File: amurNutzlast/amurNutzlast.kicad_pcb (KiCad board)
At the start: 2 copper layers, 90 parts, among them J1 Conn_01x08, J2 USB_A, J3 Conn_01x02, J5 Conn_01x07, J6 Conn_01x06, J7 Conn_01x07, J8 Conn_01x20, U1 ICE40HX1K-TQ144, U3 LD1117S33TR_SOT223, U4 FT2232HL, U5 93LCxxA, U6 W25Q128JVS, X1 SG-7050CAN, Y1 12MHz

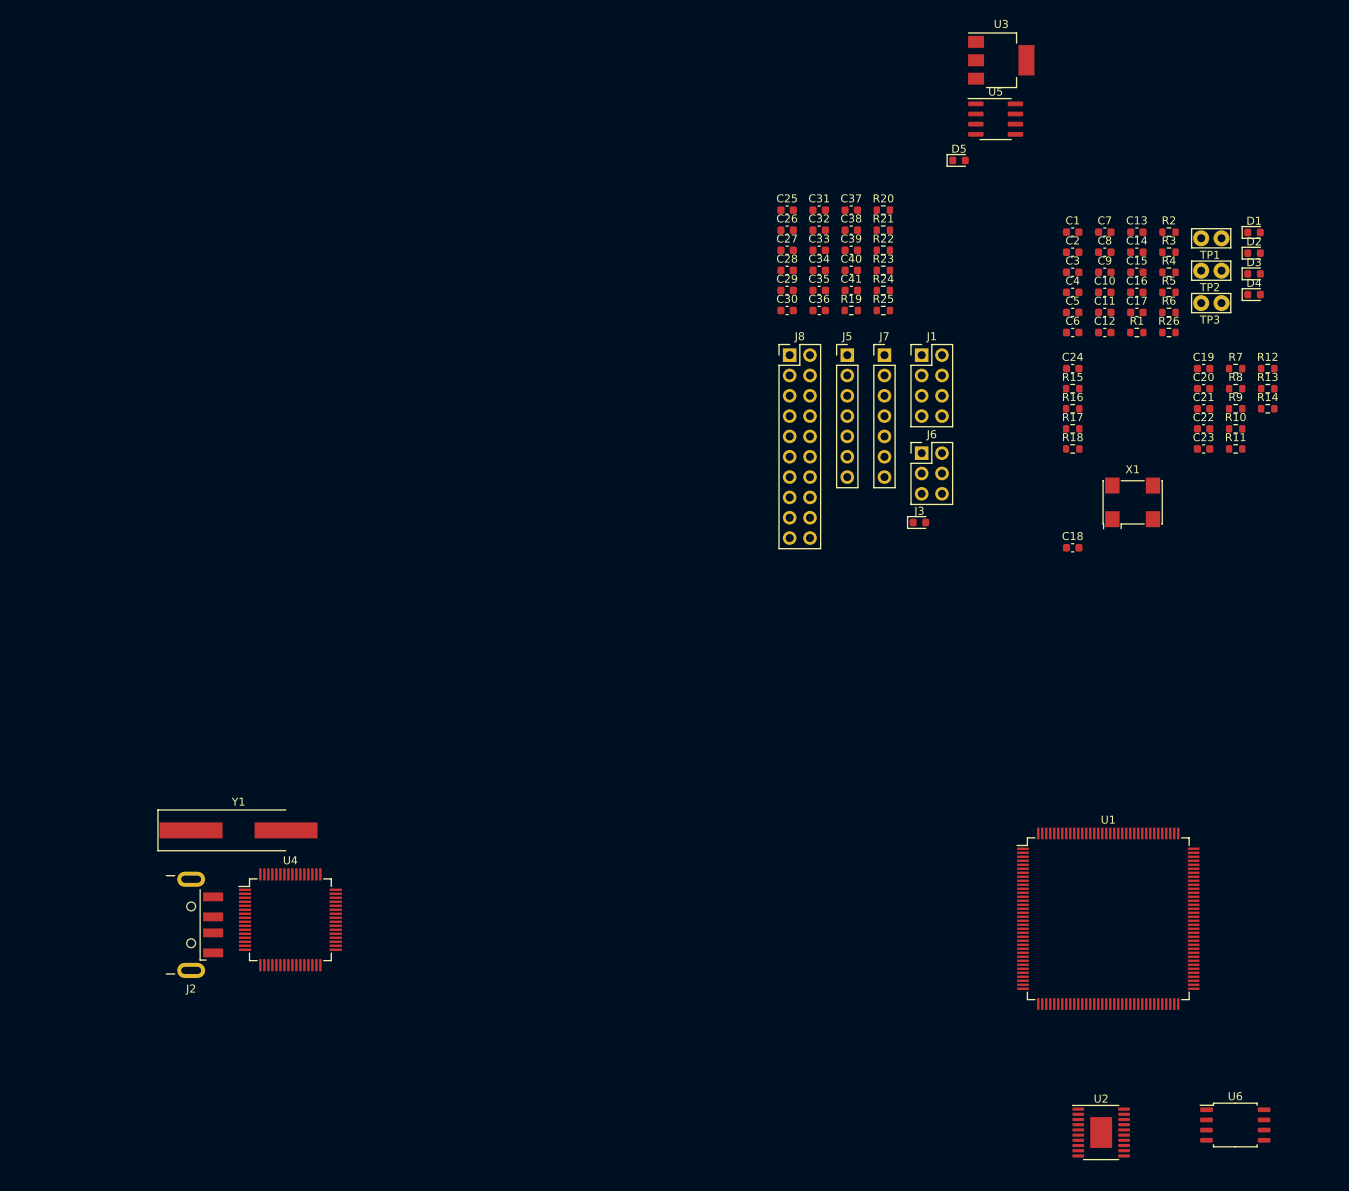
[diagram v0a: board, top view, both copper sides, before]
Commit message: deleted 3.3 converter for ftdi and moved USB to a hierarhical sheet
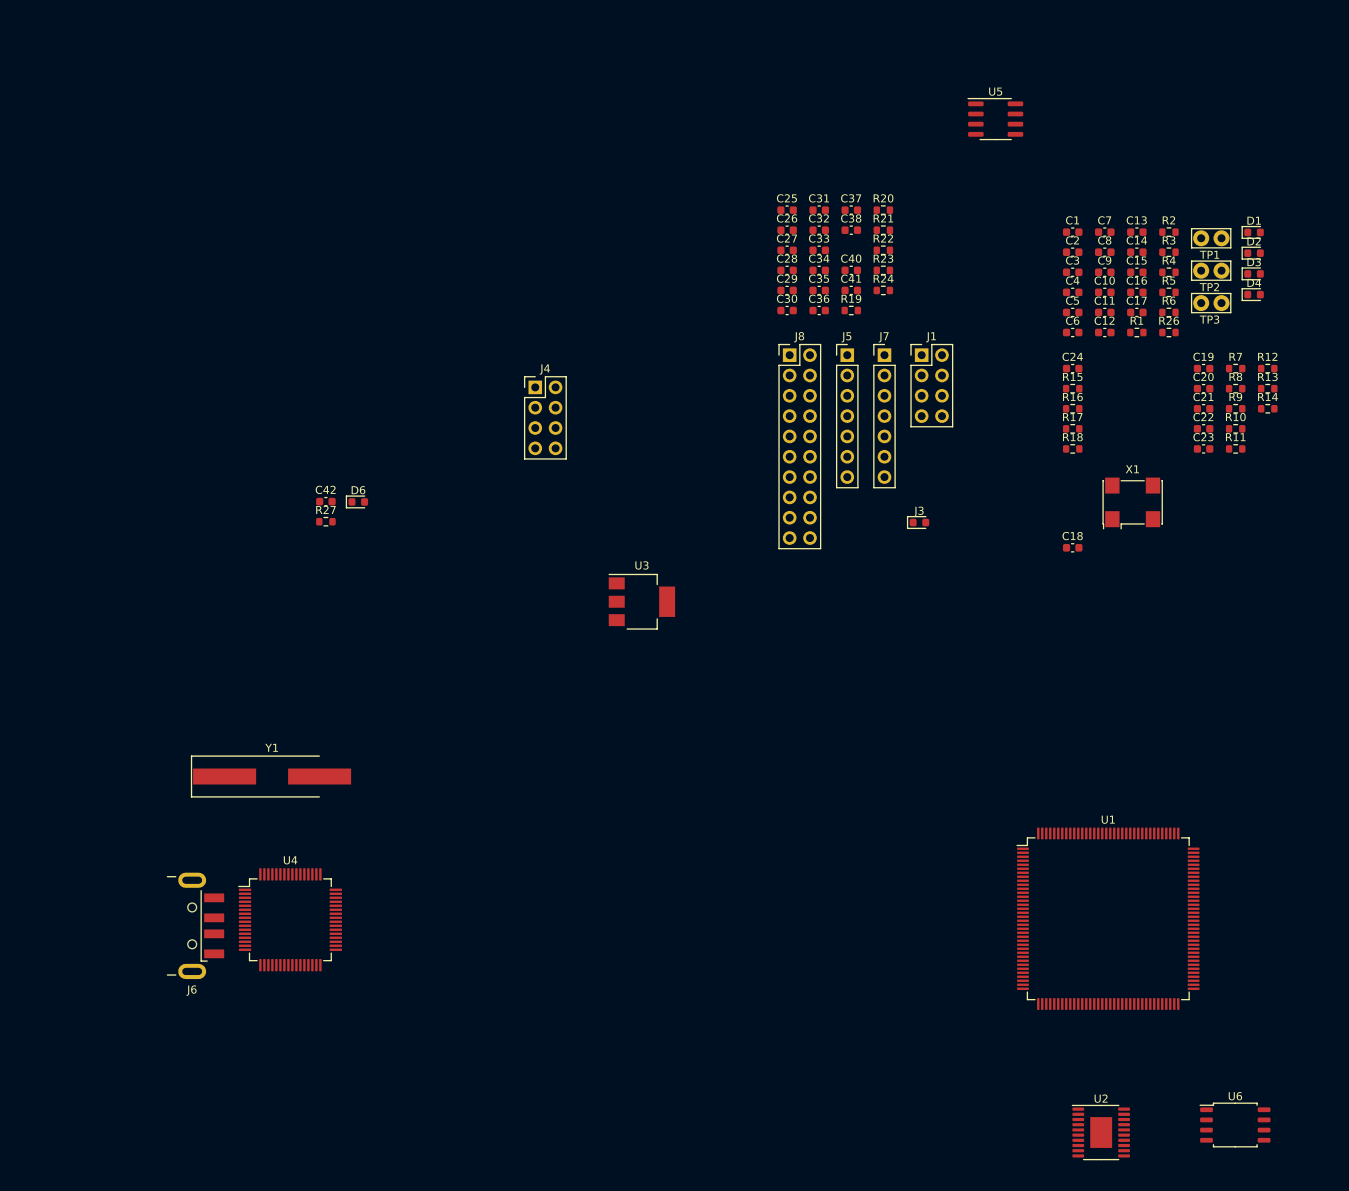
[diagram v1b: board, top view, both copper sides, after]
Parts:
- removed C39: 0.1µF, Capacitor_SMD:C_0603_1608Metric
- removed D5: LED_Small, LED_SMD:LED_0603_1608Metric
- removed J2: USB_A, Connector_USB:USB_A_CNCTech_1001-011-01101_Horizontal
- removed R25: 500, Resistor_SMD:R_0603_1608Metric
- added C42: 0.1µF, Capacitor_SMD:C_0603_1608Metric, F.Cu at (88.6, 47.8)
- added D6: LED_Small, LED_SMD:LED_0603_1608Metric, F.Cu at (92.7, 47.8)
- added J4: Conn_01x08, Connector_PinHeader_2.54mm:PinHeader_2x04_P2.54mm_Vertical, F.Cu at (114.8, 33.5)
- added R27: 500, Resistor_SMD:R_0603_1608Metric, F.Cu at (88.6, 50.3)
- J6: value Conn_01x06 -> USB_A; footprint Connector_PinHeader_2.54mm:PinHeader_2x03_P2.54mm_Vertical -> Connector_USB:USB_A_CNCTech_1001-011-01101_Horizontal
- moved J6 114.5 mm to (65.0, 100.8), turned to 180 degrees
- moved U3 81.2 mm to (128.1, 60.3)
- moved Y1 7.93 mm to (81.9, 82.2)
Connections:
- C23 pad 1: +5V -> VBUS
- C25 pad 2: GND -> GND1
- C26 pad 2: GND -> GND1
- C27 pad 2: GND -> GND1
- C28 pad 2: GND -> GND1
- C29 pad 2: GND -> GND1
- C30 pad 2: GND -> GND1
- C31 pad 2: GND -> GND1
- C32 pad 2: GND -> GND1
- C33 pad 2: GND -> GND1
- C34 pad 2: GND -> GND1
- C35 pad 2: GND -> GND1
- C36 pad 2: GND -> GND1
- C37 pad 2: GND -> GND1
- C38 pad 2: GND -> GND1
- C40 pad 2: GND -> GND1
- C41 pad 2: GND -> GND1
- J3 pad 2: +5V -> VBUS
- J6 pad 1: /ftdi/ICE_SS -> VBUS
- J6 pad 2: /ftdi/ICE_CLK -> /ftdi/DM
- J6 pad 3: /ftdi/ICE_MOSI -> /ftdi/DP
- J6 pad 4: /ftdi/ICE_MISO -> GND1
- J6 pad 5: /ftdi/ICE_CDONE -> GND1
- R23 pad 1: GND -> GND1
- R7 pad 1: +5V -> VBUS
- R8 pad 1: +5V -> VBUS
- U2 pad 11: +5V -> VBUS
- U2 pad 13: +5V -> VBUS
- U2 pad 14: +5V -> VBUS
- U2 pad 17: +5V -> VBUS
- U2 pad 18: +5V -> VBUS
- U2 pad 20: +5V -> VBUS
- U3 pad 1: GND -> GND1
- U4 pad 1: GND -> GND1
- U4 pad 10: GND -> GND1
- U4 pad 11: GND -> GND1
- U4 pad 13: GND -> GND1
- U4 pad 15: GND -> GND1
- U4 pad 25: GND -> GND1
- U4 pad 35: GND -> GND1
- U4 pad 47: GND -> GND1
- U4 pad 5: GND -> GND1
- U4 pad 51: GND -> GND1
- U5 pad 5: GND -> GND1

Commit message: layout ftdi placement
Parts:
- removed C40: 0.1µF, Capacitor_SMD:C_0603_1608Metric
- removed C41: 10µF, Capacitor_SMD:C_0603_1608Metric
- removed U3: LD1117S33TR_SOT223, Package_TO_SOT_SMD:SOT-223-3_TabPin2
- added C39: 0.1µF, Capacitor_SMD:C_0603_1608Metric, B.Cu at (99.1, 111.8)
- added C43: 10µF, Capacitor_SMD:C_0603_1608Metric, B.Cu at (96.5, 105.4)
- added U7: LD1117S33TR_SOT223, Package_TO_SOT_SMD:SOT-223-3_TabPin2, F.Cu at (101.6, 107.2)
- C25, C26, C27, C28, C29, C30, C31, C32, C33, C34, C35, C36, C37, C38, C42, R19, R20, R21, R22, R23, R24, R27: moved to B.Cu
- Y1: value 12MHz -> Crystal_GND24_Small; footprint Crystal:Crystal_SMD_HC49-SD_HandSoldering -> Crystal:Crystal_SMD_3225-4Pin_3.2x2.5mm
- moved U5 118.8 mm to (96.8, 91.7)
- moved R24 113.0 mm to (80.8, 103.6)
- moved C37 112.6 mm to (74.2, 90.4), turned to 90 degrees
- moved C32 112.3 mm to (80.8, 102.1)
- moved R23 111.5 mm to (80.8, 99.1), turned to 180 degrees
- moved C31 110.7 mm to (80.8, 97.5)
- moved C33 109.2 mm to (80.8, 100.6)
- moved C26 107.3 mm to (87.1, 103.4), turned to 90 degrees
- moved C27 107.1 mm to (83.1, 102.9), turned to 90 degrees
- moved C38 106.3 mm to (80.8, 90.7), turned to -90 degrees
- moved J1 101.3 mm to (155.4, 130.6), turned to 90 degrees
- moved C34 100.4 mm to (86.9, 96.8), turned to -90 degrees
- moved R20 100.3 mm to (98.3, 91.7), turned to 180 degrees
- moved C28 100.0 mm to (86.9, 99.3), turned to 180 degrees
- moved R21 99.5 mm to (98.3, 93.2), turned to 180 degrees
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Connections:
- C23 pad 1: VBUS -> +5V
- J3 pad 1: GND -> +5V
- J7 pad 1: /fpga/FTDI_RTS -> /fpga/FTDI_DCD
- J7 pad 2: /fpga/FTDI_TX -> /fpga/FTDI_DSR
- J7 pad 3: /fpga/FTDI_RX -> /fpga/FTDI_DTR
- J7 pad 4: /fpga/FTDI_DCD -> /fpga/FTDI_CTS
- J7 pad 5: /fpga/FTDI_DSR -> /fpga/FTDI_RTS
- J7 pad 6: /fpga/FTDI_DTR -> /fpga/FTDI_TX
- J7 pad 7: /fpga/FTDI_CTS -> /fpga/FTDI_RX
- R7 pad 1: VBUS -> +5V
- R8 pad 1: VBUS -> +5V
- U2 pad 11: VBUS -> +5V
- U2 pad 13: VBUS -> +5V
- U2 pad 14: VBUS -> +5V
- U2 pad 17: VBUS -> +5V
- U2 pad 18: VBUS -> +5V
- U2 pad 20: VBUS -> +5V
- Y1 pad 1: Net-(U4-OSCO) -> Net-(U4-OSCI)
- Y1 pad 2: Net-(U4-OSCI) -> GND1

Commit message: ftdi layout continuation
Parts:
- moved J1 35.6 mm to (121.4, 120.1)
- moved J4 14.3 mm to (99.0, 106.7), turned to -90 degrees
- moved J7 13.3 mm to (118.1, 84.1)
- moved C43 8.75 mm to (104.4, 109.2)
- moved U7 8.75 mm to (109.5, 111.0)
- moved C39 8.75 mm to (106.9, 115.6)
- moved C38 7.19 mm to (73.6, 91.4), turned to 90 degrees
- moved U1 6.71 mm to (150.6, 100.3)
- moved R22 6.41 mm to (94.7, 89.4)
- moved C37 6.18 mm to (80.2, 91.7), turned to -90 degrees
- moved C25 4.22 mm to (94.7, 87.9)
- moved D6 3.79 mm to (82.3, 112.0)
- moved R20 3.64 mm to (94.7, 90.9)
- moved R21 3.64 mm to (94.7, 92.5)
- moved U5 3.64 mm to (93.2, 90.9)
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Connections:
- net /ftdi/DM renamed /usb/-
- net /ftdi/DP renamed /usb/+
- J5 pad 1: /ftdi/CTS -> /ftdi/DCD
- J5 pad 2: /ftdi/DTR -> /ftdi/DSR
- J5 pad 3: /ftdi/DSR -> /ftdi/DTR
- J5 pad 4: /ftdi/DCD -> /ftdi/CTS
- J5 pad 5: /ftdi/RX -> /ftdi/RTS
- J5 pad 7: /ftdi/RTS -> /ftdi/RX
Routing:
- net /ftdi/DCD: track 0.00 -> 23.3 mm
- net /ftdi/DSR: track 0.00 -> 22.5 mm
- net /ftdi/DTR: track 0.00 -> 21.6 mm
- net /ftdi/CTS: track 0.00 -> 21.0 mm
- net /ftdi/RTS: track 0.00 -> 20.2 mm
- net /ftdi/TX: track 0.00 -> 19.3 mm
- net /ftdi/RX: track 0.00 -> 18.5 mm
- net /usb/-: track 0.00 -> 11.7 mm
- net /usb/+: track 0.00 -> 11.5 mm
- net Net-(U4-OSCI): track 0.00 -> 7.75 mm
- net Net-(U4-OSCO): track 0.00 -> 6.64 mm
- net +3.3VP: track 0.00 -> 1.86 mm, vias 0 -> 1

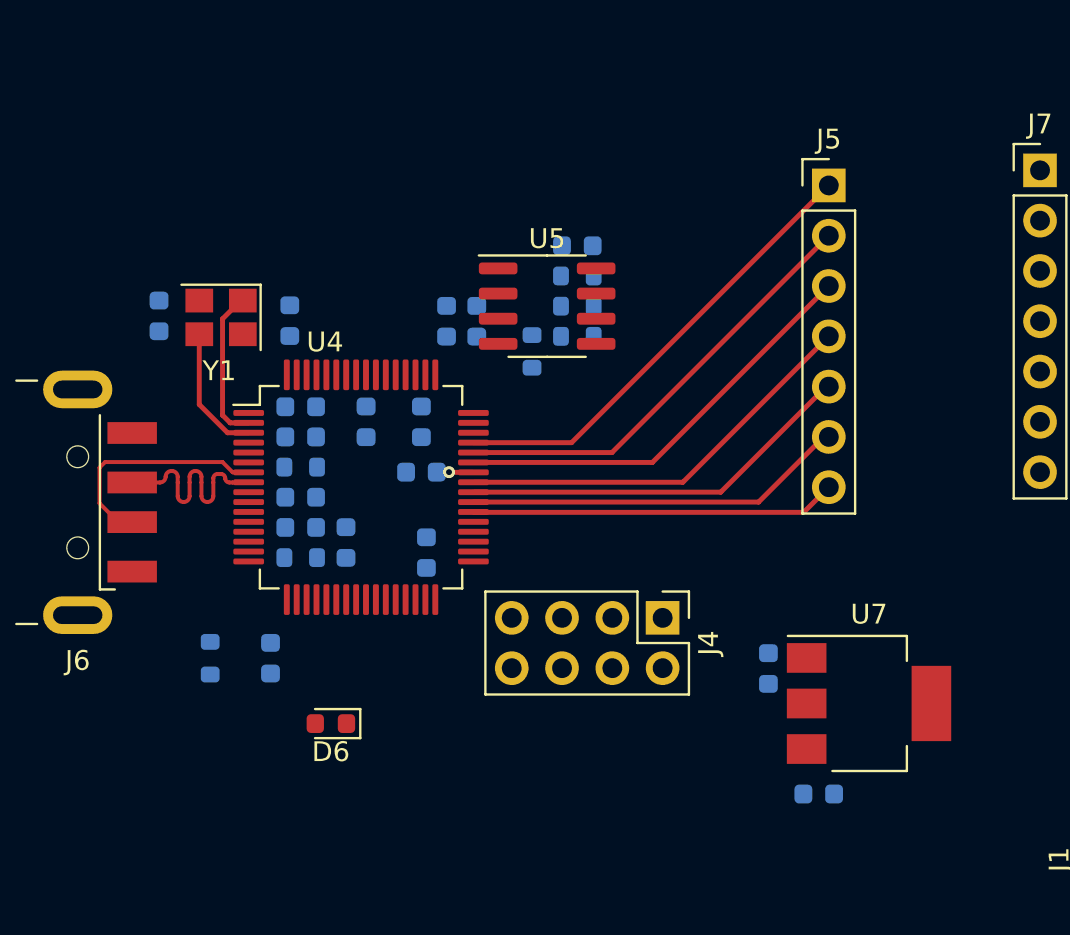
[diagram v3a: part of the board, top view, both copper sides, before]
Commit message: ftdi layout finish
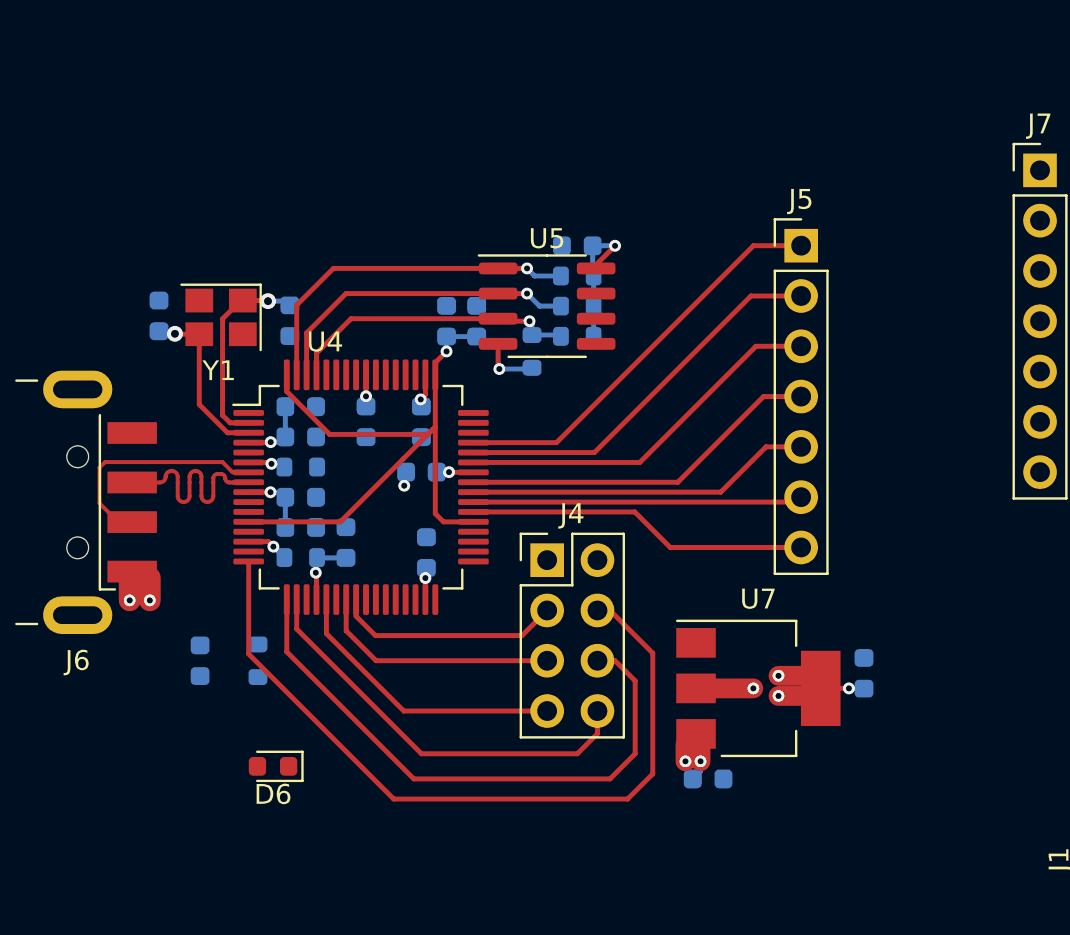
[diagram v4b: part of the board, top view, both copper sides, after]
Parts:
- moved J4 6.52 mm to (93.2, 103.8), turned to 0 degrees
- moved U7 5.64 mm to (103.9, 110.2)
- moved C39 5.64 mm to (101.3, 114.8)
- moved C43 4.83 mm to (109.2, 109.5)
- moved D6 3.63 mm to (79.4, 114.2)
- moved C42 3.56 mm to (75.7, 108.8)
- moved J5 3.35 mm to (106.0, 87.9)
- moved R27 2.42 mm to (78.6, 108.8)
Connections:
- C25 pad 1: +3.3V -> +3.3VP
- J4 pad 3: /ftdi/ICE_SS -> /ftdi/ICE_CREST
- J4 pad 5: /ftdi/ICE_MOSI -> /ftdi/ICE_CDONE
- J4 pad 6: /ftdi/ICE_MISO -> /ftdi/ICE_MOSI
- J4 pad 7: /ftdi/ICE_CDONE -> /ftdi/ICE_SS
- J4 pad 8: /ftdi/ICE_CREST -> /ftdi/ICE_MISO
- R20 pad 1: +3.3V -> +3.3VP
- R21 pad 1: +3.3V -> +3.3VP
- R22 pad 1: +3.3V -> +3.3VP
- U5 pad 8: +3.3V -> +3.3VP
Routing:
- net /ftdi/ICE_CLK: track 0.00 -> 38.4 mm
- net +1V8: track 0.00 -> 33.6 mm, vias 0 -> 1
- net +3.3VP: track 1.86 -> 35.3 mm, vias 1 -> 12
- net /ftdi/ICE_MOSI: track 0.00 -> 29.4 mm
- net /ftdi/ICE_MISO: track 0.00 -> 20.8 mm
- net /ftdi/CS_FTDI: track 0.00 -> 17.8 mm, vias 0 -> 1
- net Net-(U4-EECLK): track 0.00 -> 16.0 mm, vias 0 -> 1
- net Net-(U4-EEDATA): track 0.00 -> 14.9 mm, vias 0 -> 1
- net /ftdi/ICE_SS: track 0.00 -> 14.5 mm
- net /ftdi/ICE_CDONE: track 0.00 -> 12.4 mm
- net /ftdi/ICE_CREST: track 0.00 -> 11.4 mm
- net VBUS: track 0.00 -> 8.54 mm, vias 0 -> 4
- net Net-(U5-DO): track 0.00 -> 2.97 mm, vias 0 -> 1
- net /ftdi/RTS: track 20.2 -> 17.5 mm
- net /ftdi/DCD: track 23.3 -> 20.7 mm
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- added copper zone on In2.Cu, net +3.3VP
- added copper zone on In1.Cu, net GND1
- added copper zone on In2.Cu, net VBUS
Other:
- copper layers 2 -> 4

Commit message: started FPGA
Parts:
- removed J3: Conn_01x02, LED_SMD:LED_0603_1608Metric
- removed R26: 0, Resistor_SMD:R_0603_1608Metric
- C1, C10, C11, C12, C13, C14, C15, C16, C17, C18, C2, C24, C3, C4, C5, C6, C7, C8, C9, D1, R1, R15, R16, R17, R18, R2, R3, R4, R5, R6: moved to B.Cu
- TP1, TP2, TP3: footprint TestPoint:TestPoint_Bridge_Pitch2.54mm_Drill1.0mm -> TestPoint:TestPoint_Pad_D2.5mm
- moved R2 115.7 mm to (137.6, 115.2)
- moved R3 112.2 mm to (137.6, 113.5), turned to 180 degrees
- moved C13 111.2 mm to (133.8, 110.1), turned to 180 degrees
- moved C9 107.4 mm to (142.7, 117.5), turned to 180 degrees
- moved D1 102.2 mm to (161.4, 106.8)
- moved C14 100.2 mm to (153.8, 110.0)
- moved TP1 99.4 mm to (177.1, 112.0)
- moved C10 98.5 mm to (128.4, 101.5), turned to 180 degrees
- moved C3 98.1 mm to (153.7, 113.1)
- moved R1 98.1 mm to (128.4, 103.0)
- moved R16 97.1 mm to (125.8, 115.4), turned to 180 degrees
- moved C5 97.0 mm to (131.4, 106.9), turned to 180 degrees
- moved C15 96.5 mm to (131.6, 96.0), turned to 180 degrees
- moved TP2 96.3 mm to (172.9, 111.9)
- moved C24 96.2 mm to (127.5, 110.5), turned to 180 degrees
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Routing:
- net GND1: track 0.72 -> 44.1 mm, vias 1 -> 34
- net VBUS: track 8.54 -> 15.0 mm
- net Net-(D6-A): track 0.00 -> 4.53 mm, vias 0 -> 1
- net /ICE_CLK: track 0.00 -> 2.77 mm
- net /fpga/FTDI_DCD: track 0.00 -> 1.18 mm

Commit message: placement finished
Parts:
- added C40: 0.1µF, Capacitor_SMD:C_0603_1608Metric, B.Cu at (152.5, 90.3)
- added C41: 10µF, Capacitor_SMD:C_0603_1608Metric, B.Cu at (152.5, 88.8)
- added C44: 0.1µF, Capacitor_SMD:C_0603_1608Metric, B.Cu at (158.4, 108.5)
- added C45: 10µF, Capacitor_SMD:C_0603_1608Metric, B.Cu at (158.4, 107.0)
- added C46: 0.1µF, Capacitor_SMD:C_0603_1608Metric, B.Cu at (134.5, 112.0)
- added C47: 10µF, Capacitor_SMD:C_0603_1608Metric, B.Cu at (134.5, 113.5)
- added C48: 0.1µF, Capacitor_SMD:C_0603_1608Metric, B.Cu at (129.8, 96.0)
- added C49: 10µF, Capacitor_SMD:C_0603_1608Metric, B.Cu at (129.8, 97.5)
- added J2: Conn_02x02_Counter_Clockwise, Connector_PinHeader_2.54mm:PinHeader_2x02_P2.54mm_Vertical, F.Cu at (114.6, 113.1)
- C19, C20, C21, C22, C23, R10, R11, R12, R13, R14, R7, R8, R9: moved to B.Cu
- J1: value Conn_01x08 -> Conn_01x06; footprint Connector_PinHeader_2.54mm:PinHeader_2x04_P2.54mm_Vertical -> Connector_PinHeader_2.54mm:PinHeader_2x03_P2.54mm_Vertical
- moved R7 92.7 mm to (174.5, 119.6), turned to 180 degrees
- moved R8 92.4 mm to (168.1, 119.5)
- moved C19 84.2 mm to (172.8, 111.5)
- moved R12 83.9 mm to (174.6, 108.8)
- moved C23 82.7 mm to (166.3, 117.5), turned to 180 degrees
- moved R13 82.4 mm to (176.4, 110.5)
- moved C21 80.8 mm to (170.6, 112.1), turned to -90 degrees
- moved C20 80.4 mm to (169.8, 108.8), turned to 180 degrees
- moved R11 78.4 mm to (168.9, 112.1), turned to -90 degrees
- moved R14 77.9 mm to (174.7, 107.3), turned to 180 degrees
- moved R10 76.0 mm to (169.8, 107.3), turned to 180 degrees
- moved R9 74.9 mm to (174.6, 105.8)
- moved C22 74.1 mm to (172.3, 108.0), turned to 90 degrees
- moved R5 14.4 mm to (160.7, 86.8)
- moved TP3 10.0 mm to (188.4, 118.8)
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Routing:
- net +3.3V: track 0.00 -> 46.1 mm, vias 0 -> 9
- net /fpga/FTDI_RX: track 0.00 -> 33.4 mm
- net /fpga/FTDI_TX: track 0.00 -> 33.0 mm
- net /fpga/FTDI_RTS: track 0.00 -> 32.5 mm
- net /fpga/FTDI_CTS: track 0.00 -> 32.5 mm
- net /fpga/FTDI_DTR: track 0.00 -> 32.0 mm
- net /fpga/FTDI_DSR: track 0.00 -> 31.6 mm
- net /fpga/FTDI_DCD: track 1.18 -> 32.4 mm
- net Net-(D4-A): track 0.00 -> 20.9 mm
- net Net-(D3-A): track 0.00 -> 14.9 mm
- net +1V2: track 0.00 -> 10.4 mm, vias 0 -> 4
- net Net-(D2-A): track 0.00 -> 8.65 mm
- net GNDD: track 0.00 -> 7.40 mm, vias 0 -> 1
- net Net-(D1-K): track 0.00 -> 6.24 mm, vias 0 -> 1
- net Net-(U1E-VCCPLL): track 0.00 -> 6.19 mm, vias 0 -> 1
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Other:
- board outline added: 126 x 39 mm
